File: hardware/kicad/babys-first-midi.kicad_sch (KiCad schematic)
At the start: 22 parts, among them J1 RJ45_FEMALE, J2 TRS TYPE A, Q1 IRLZ44N, Q2 IRLZ44N, Q3 IRLZ44N, Q4 IRLZ44N, Q5 IRLZ44N, U1 Pimoroni Tiny 2350

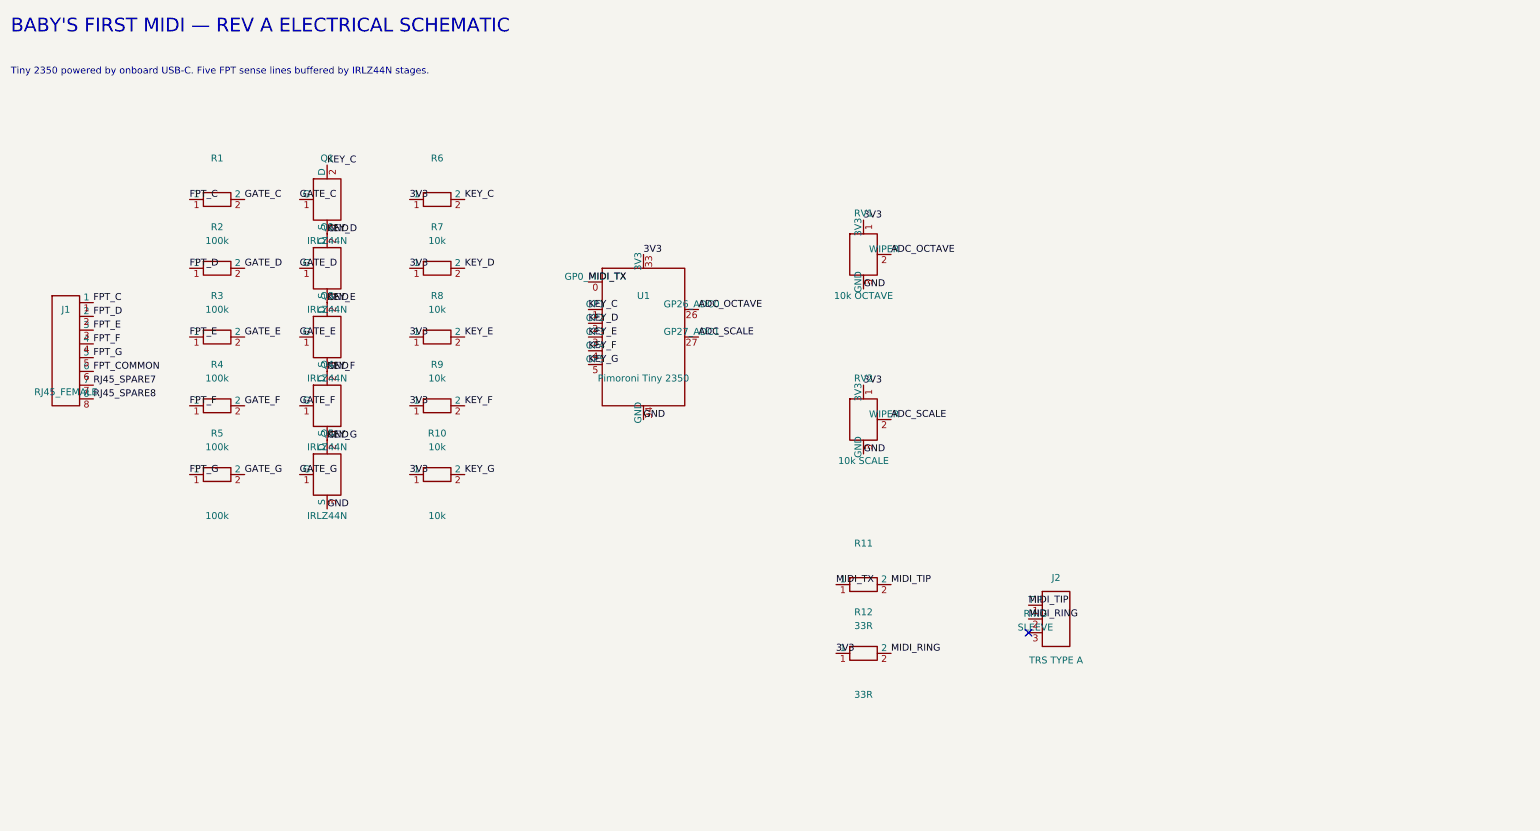
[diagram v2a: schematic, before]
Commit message: Wire Rev A schematic connections
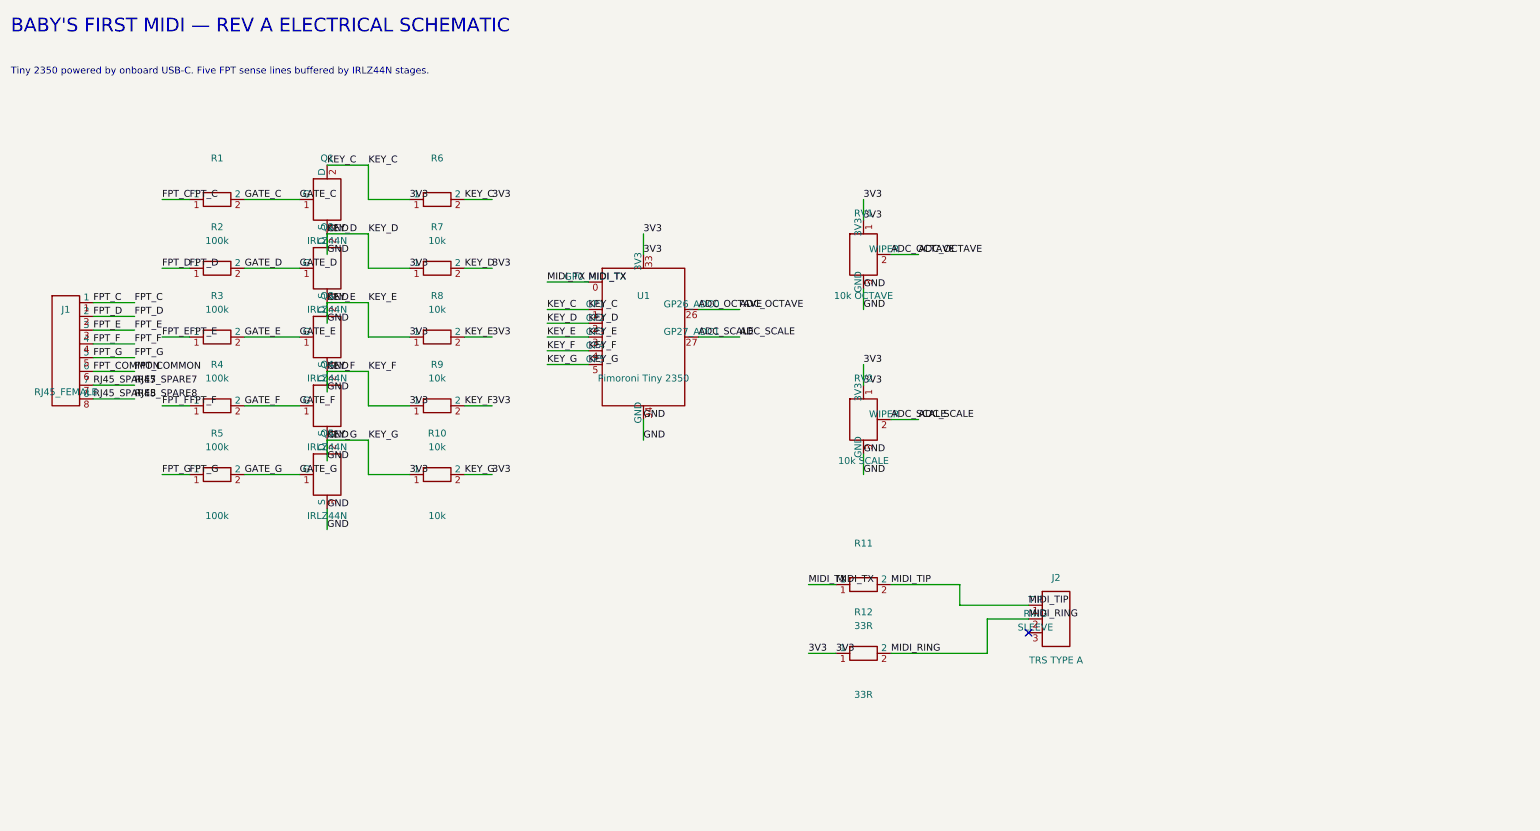
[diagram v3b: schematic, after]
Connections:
- net GND is gone; now on net 3V3: Q1.3 (S), Q2.2 (D), Q2.3 (S), Q3.2 (D), Q3.3 (S), Q4.2 (D), Q4.3 (S), Q5.2 (D), Q5.3 (S), R10.2, R7.2, R8.2, R9.2, RV1.3 (GND), RV2.3 (GND), U1.2 (GP2), U1.3 (GP3), U1.34 (GND), U1.4 (GP4), U1.5 (GP5)
- net KEY_C is gone; now on net 3V3: Q1.2 (D), R6.2, U1.1 (GP1)
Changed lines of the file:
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@@
   (label "MIDI_TIP" (at 208.28 120.65 0) (effects (font (size 1.27 1.27)) (justify left bottom)))
   (label "MIDI_RING" (at 208.28 123.19 0) (effects (font (size 1.27 1.27)) (justify left bottom)))
+  (wire (pts (xy 48.26 45.72) (xy 53.34 45.72)) (stroke (width 0) (type default)))
+  (label "FPT_C" (at 48.26 45.72 0) (effects (font (size 1.27 1.27)) (justify left bottom)))
+  (wire (pts (xy 63.5 45.72) (xy 73.66 45.72)) (stroke (width 0) (type default)))
+  (wire (pts (xy 78.74 39.37) (xy 86.36 39.37) (xy 86.36 45.72) (xy 93.98 45.72)) (stroke (width 0) (type default)))
+  (label "KEY_C" (at 86.36 39.37 0) (effects (font (size 1.27 1.27)) (justify left bottom)))
+  (wire (pts (xy 104.14 45.72) (xy 109.22 45.72)) (stroke (width 0) (type default)))
+  (label "3V3" (at 109.22 45.72 0) (effects (font (size 1.27 1.27)) (justify left bottom)))
+  (wire (pts (xy 78.74 52.07) (xy 78.74 55.88)) (stroke (width 0) (type default)))
+  (label "GND" (at 78.74 55.88 0) (effects (font (size 1.27 1.27)) (justify left bottom)))
+  (wire (pts (xy 48.26 58.42) (xy 53.34 58.42)) (stroke (width 0) (type default)))
+  (label "FPT_D" (at 48.26 58.42 0) (effects (font (size 1.27 1.27)) (justify left bottom)))
+  (wire (pts (xy 63.5 58.42) (xy 73.66 58.42)) (stroke (width 0) (type default)))
+  (wire (pts (xy 78.74 52.07) (xy 86.36 52.07) (xy 86.36 58.42) (xy 93.98 58.42)) (stroke (width 0) (type default)))
+  (label "KEY_D" (at 86.36 52.07 0) (effects (font (size 1.27 1.27)) (justify left bottom)))
+  (wire (pts (xy 104.14 58.42) (xy 109.22 58.42)) (stroke (width 0) (type default)))
+  (label "3V3" (at 109.22 58.42 0) (effects (font (size 1.27 1.27)) (justify left bottom)))
+  (wire (pts (xy 78.74 64.77) (xy 78.74 68.58)) (stroke (width 0) (type default)))
+  (label "GND" (at 78.74 68.58 0) (effects (font (size 1.27 1.27)) (justify left bottom)))
+  (wire (pts (xy 48.26 71.12) (xy 53.34 71.12)) (stroke (width 0) (type default)))
+  (label "FPT_E" (at 48.26 71.12 0) (effects (font (size 1.27 1.27)) (justify left bottom)))
+  (wire (pts (xy 63.5 71.12) (xy 73.66 71.12)) (stroke (width 0) (type default)))
+  (wire (pts (xy 78.74 64.77000000000001) (xy 86.36 64.77000000000001) (xy 86.36 71.12) (xy 93.98 71.12)) (stroke (width 0) (type default)))
+  (label "KEY_E" (at 86.36 64.77000000000001 0) (effects (font (size 1.27 1.27)) (justify left bottom)))
+  (wire (pts (xy 104.14 71.12) (xy 109.22 71.12)) (stroke (width 0) (type default)))
+  (label "3V3" (at 109.22 71.12 0) (effects (font (size 1.27 1.27)) (justify left bottom)))
+  (wire (pts (xy 78.74 77.47) (xy 78.74 81.28)) (stroke (width 0) (type default)))
+  (label "GND" (at 78.74 81.28 0) (effects (font (size 1.27 1.27)) (justify left bottom)))
+  (wire (pts (xy 48.26 83.82) (xy 53.34 83.82)) (stroke (width 0) (type default)))
+  (label "FPT_F" (at 48.26 83.82 0) (effects (font (size 1.27 1.27)) (justify left bottom)))
+  (wire (pts (xy 63.5 83.82) (xy 73.66 83.82)) (stroke (width 0) (type default)))
+  (wire (pts (xy 78.74 77.47) (xy 86.36 77.47) (xy 86.36 83.82) (xy 93.98 83.82)) (stroke (width 0) (type default)))
+  (label "KEY_F" (at 86.36 77.47 0) (effects (font (size 1.27 1.27)) (justify left bottom)))
+  (wire (pts (xy 104.14 83.82) (xy 109.22 83.82)) (stroke (width 0) (type default)))
+  (label "3V3" (at 109.22 83.82 0) (effects (font (size 1.27 1.27)) (justify left bottom)))
+  (wire (pts (xy 78.74 90.16999999999999) (xy 78.74 93.97999999999999)) (stroke (width 0) (type default)))
+  (label "GND" (at 78.74 93.97999999999999 0) (effects (font (size 1.27 1.27)) (justify left bottom)))
+  (wire (pts (xy 48.26 96.52) (xy 53.34 96.52)) (stroke (width 0) (type default)))
+  (label "FPT_G" (at 48.26 96.52 0) (effects (font (size 1.27 1.27)) (justify left bottom)))
+  (wire (pts (xy 63.5 96.52) (xy 73.66 96.52)) (stroke (width 0) (type default)))
+  (wire (pts (xy 78.74 90.17) (xy 86.36 90.17) (xy 86.36 96.52) (xy 93.98 96.52)) (stroke (width 0) (type default)))
+  (label "KEY_G" (at 86.36 90.17 0) (effects (font (size 1.27 1.27)) (justify left bottom)))
+  (wire (pts (xy 104.14 96.52) (xy 109.22 96.52)) (stroke (width 0) (type default)))
+  (label "3V3" (at 109.22 96.52 0) (effects (font (size 1.27 1.27)) (justify left bottom)))
+  (wire (pts (xy 78.74 102.86999999999999) (xy 78.74 106.67999999999999)) (stroke (width 0) (type default)))
+  (label "GND" (at 78.74 106.67999999999999 0) (effects (font (size 1.27 1.27)) (justify left bottom)))
+  (wire (pts (xy 35.56 64.77) (xy 43.18 64.77)) (stroke (width 0) (type default)))
+  (label "FPT_C" (at 43.18 64.77 0) (effects (font (size 1.27 1.27)) (justify left bottom)))
+  (wire (pts (xy 35.56 67.31) (xy 43.18 67.31)) (stroke (width 0) (type default)))
+  (label "FPT_D" (at 43.18 67.31 0) (effects (font (size 1.27 1.27)) (justify left bottom)))
+  (wire (pts (xy 35.56 69.85) (xy 43.18 69.85)) (stroke (width 0) (type default)))
+  (label "FPT_E" (at 43.18 69.85 0) (effects (font (size 1.27 1.27)) (justify left bottom)))
+  (wire (pts (xy 35.56 72.39) (xy 43.18 72.39)) (stroke (width 0) (type default)))
+  (label "FPT_F" (at 43.18 72.39 0) (effects (font (size 1.27 1.27)) (justify left bottom)))
+  (wire (pts (xy 35.56 74.93) (xy 43.18 74.93)) (stroke (width 0) (type default)))
+  (label "FPT_G" (at 43.18 74.93 0) (effects (font (size 1.27 1.27)) (justify left bottom)))
+  (wire (pts (xy 35.56 77.47) (xy 43.18 77.47)) (stroke (width 0) (type default)))
+  (label "FPT_COMMON" (at 43.18 77.47 0) (effects (font (size 1.27 1.27)) (justify left bottom)))
+  (wire (pts (xy 35.56 80.01) (xy 43.18 80.01)) (stroke (width 0) (type default)))
+  (label "RJ45_SPARE7" (at 43.18 80.01 0) (effects (font (size 1.27 1.27)) (justify left bottom)))
+  (wire (pts (xy 35.56 82.55) (xy 43.18 82.55)) (stroke (width 0) (type default)))
+  (label "RJ45_SPARE8" (at 43.18 82.55 0) (effects (font (size 1.27 1.27)) (justify left bottom)))
+  (wire (pts (xy 127 60.96) (xy 119.38 60.96)) (stroke (width 0) (type default)))
+  (label "MIDI_TX" (at 119.38 60.96 0) (effects (font (size 1.27 1.27)) (justify left bottom)))
+  (wire (pts (xy 127 66.04) (xy 119.38 66.04)) (stroke (width 0) (type default)))
+  (label "KEY_C" (at 119.38 66.04 0) (effects (font (size 1.27 1.27)) (justify left bottom)))
+  (wire (pts (xy 127 68.58) (xy 119.38 68.58)) (stroke (width 0) (type default)))
+  (label "KEY_D" (at 119.38 68.58 0) (effects (font (size 1.27 1.27)) (justify left bottom)))
+  (wire (pts (xy 127 71.12) (xy 119.38 71.12)) (stroke (width 0) (type default)))
+  (label "KEY_E" (at 119.38 71.12 0) (effects (font (size 1.27 1.27)) (justify left bottom)))
+  (wire (pts (xy 127 73.66) (xy 119.38 73.66)) (stroke (width 0) (type default)))
+  (label "KEY_F" (at 119.38 73.66 0) (effects (font (size 1.27 1.27)) (justify left bottom)))
+  (wire (pts (xy 127 76.2) (xy 119.38 76.2)) (stroke (width 0) (type default)))
+  (label "KEY_G" (at 119.38 76.2 0) (effects (font (size 1.27 1.27)) (justify left bottom)))
+  (wire (pts (xy 147.32 66.04) (xy 154.94 66.04)) (stroke (width 0) (type default)))
+  (label "ADC_OCTAVE" (at 154.94 66.04 0) (effects (font (size 1.27 1.27)) (justify left bottom)))
+  (wire (pts (xy 147.32 71.12) (xy 154.94 71.12)) (stroke (width 0) (type default)))
+  (label "ADC_SCALE" (at 154.94 71.12 0) (effects (font (size 1.27 1.27)) (justify left bottom)))
+  (wire (pts (xy 137.16 55.88) (xy 137.16 52.07)) (stroke (width 0) (type default)))
+  (label "3V3" (at 137.16 52.07 0) (effects (font (size 1.27 1.27)) (justify left bottom)))
+  (wire (pts (xy 137.16 86.36) (xy 137.16 90.17)) (stroke (width 0) (type default)))
+  (label "GND" (at 137.16 90.17 0) (effects (font (size 1.27 1.27)) (justify left bottom)))
+  (wire (pts (xy 177.8 49.53) (xy 177.8 45.72)) (stroke (width 0) (type default)))
+  (label "3V3" (at 177.8 45.72 0) (effects (font (size 1.27 1.27)) (justify left bottom)))
+  (wire (pts (xy 177.8 62.230000000000004) (xy 177.8 66.04)) (stroke (width 0) (type default)))
+  (label "GND" (at 177.8 66.04 0) (effects (font (size 1.27 1.27)) (justify left bottom)))
+  (wire (pts (xy 182.88000000000002 55.88) (xy 187.96 55.88)) (stroke (width 0) (type default)))
+  (label "ADC_OCTAVE" (at 187.96 55.88 0) (effects (font (size 1.27 1.27)) (justify left bottom)))
+  (wire (pts (xy 177.8 80.01) (xy 177.8 76.2)) (stroke (width 0) (type default)))
+  (label "3V3" (at 177.8 76.2 0) (effects (font (size 1.27 1.27)) (justify left bottom)))
+  (wire (pts (xy 177.8 92.71) (xy 177.8 96.52)) (stroke (width 0) (type default)))
+  (label "GND" (at 177.8 96.52 0) (effects (font (size 1.27 1.27)) (justify left bottom)))
+  (wire (pts (xy 182.88000000000002 86.36) (xy 187.96 86.36)) (stroke (width 0) (type default)))
+  (label "ADC_SCALE" (at 187.96 86.36 0) (effects (font (size 1.27 1.27)) (justify left bottom)))
+  (wire (pts (xy 172.72 116.84) (xy 167.64 116.84)) (stroke (width 0) (type default)))
+  (label "MIDI_TX" (at 167.64 116.84 0) (effects (font (size 1.27 1.27)) (justify left bottom)))
+  (wire (pts (xy 172.72 129.54) (xy 167.64 129.54)) (stroke (width 0) (type default)))
+  (label "3V3" (at 167.64 129.54 0) (effects (font (size 1.27 1.27)) (justify left bottom)))
+  (wire (pts (xy 182.88 116.84) (xy 195.58 116.84) (xy 195.58 120.65) (xy 208.28 120.65)) (stroke (width 0) (type default)))
+  (wire (pts (xy 182.88 129.54) (xy 200.66 129.54) (xy 200.66 123.19) (xy 208.28 123.19)) (stroke (width 0) (type default)))
   (no_connect (at 208.28 125.73))
   (sheet_instances (path "/" (page "1")))
